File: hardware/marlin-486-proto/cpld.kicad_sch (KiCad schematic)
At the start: 1 part, among them U2 EPM240T100

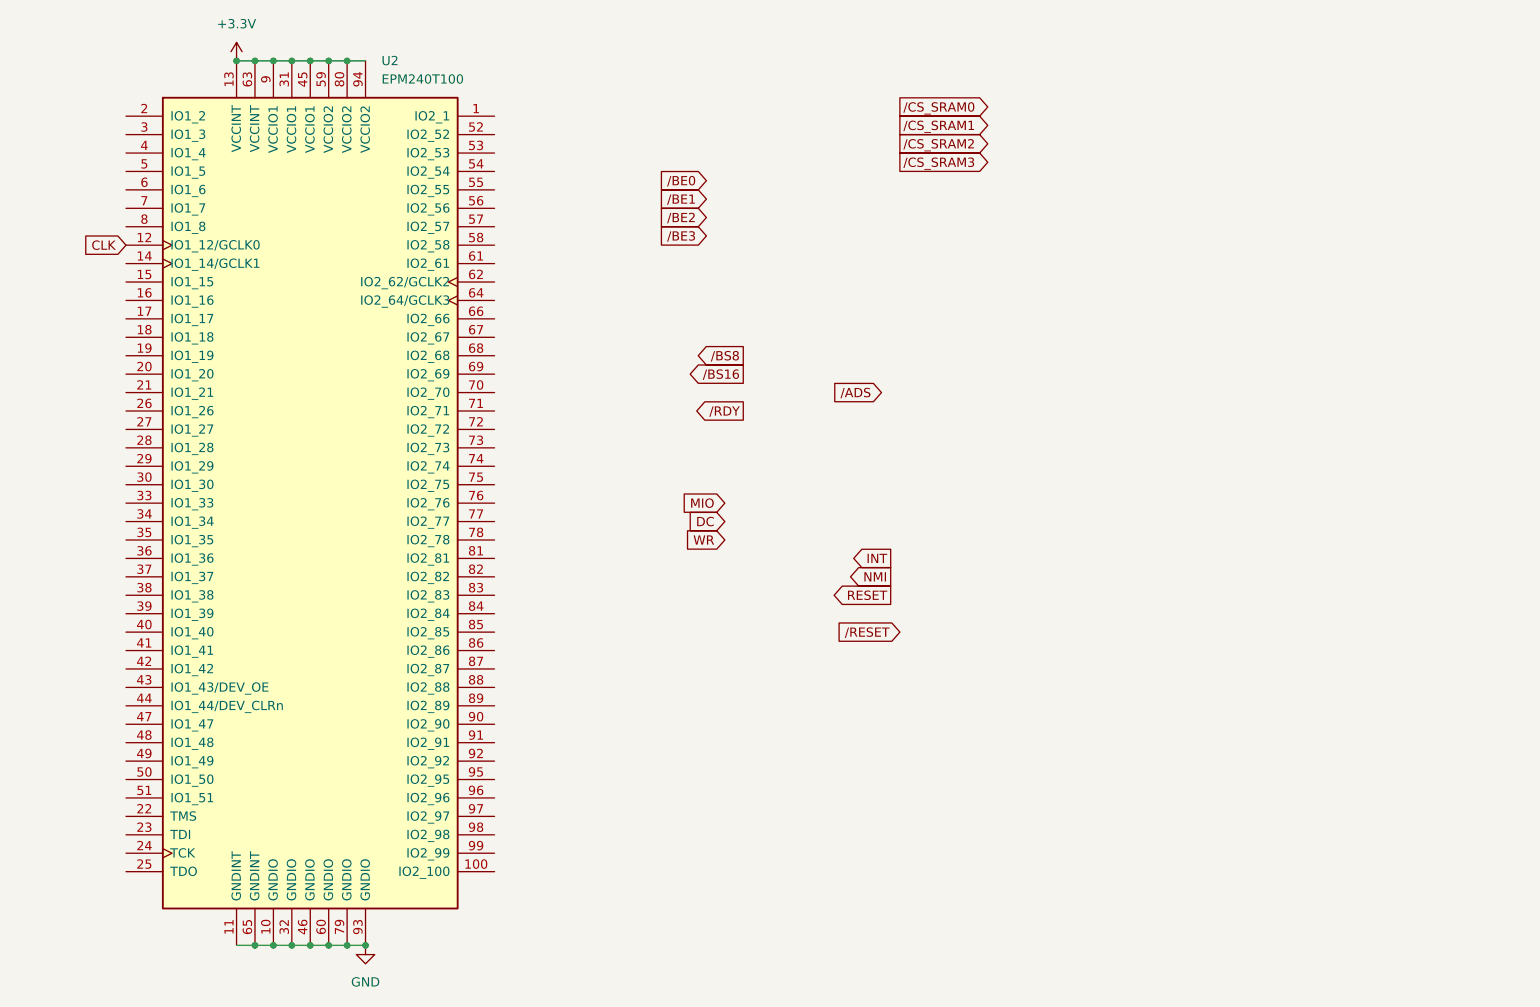
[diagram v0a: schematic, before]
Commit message: Add 16C550 symbol
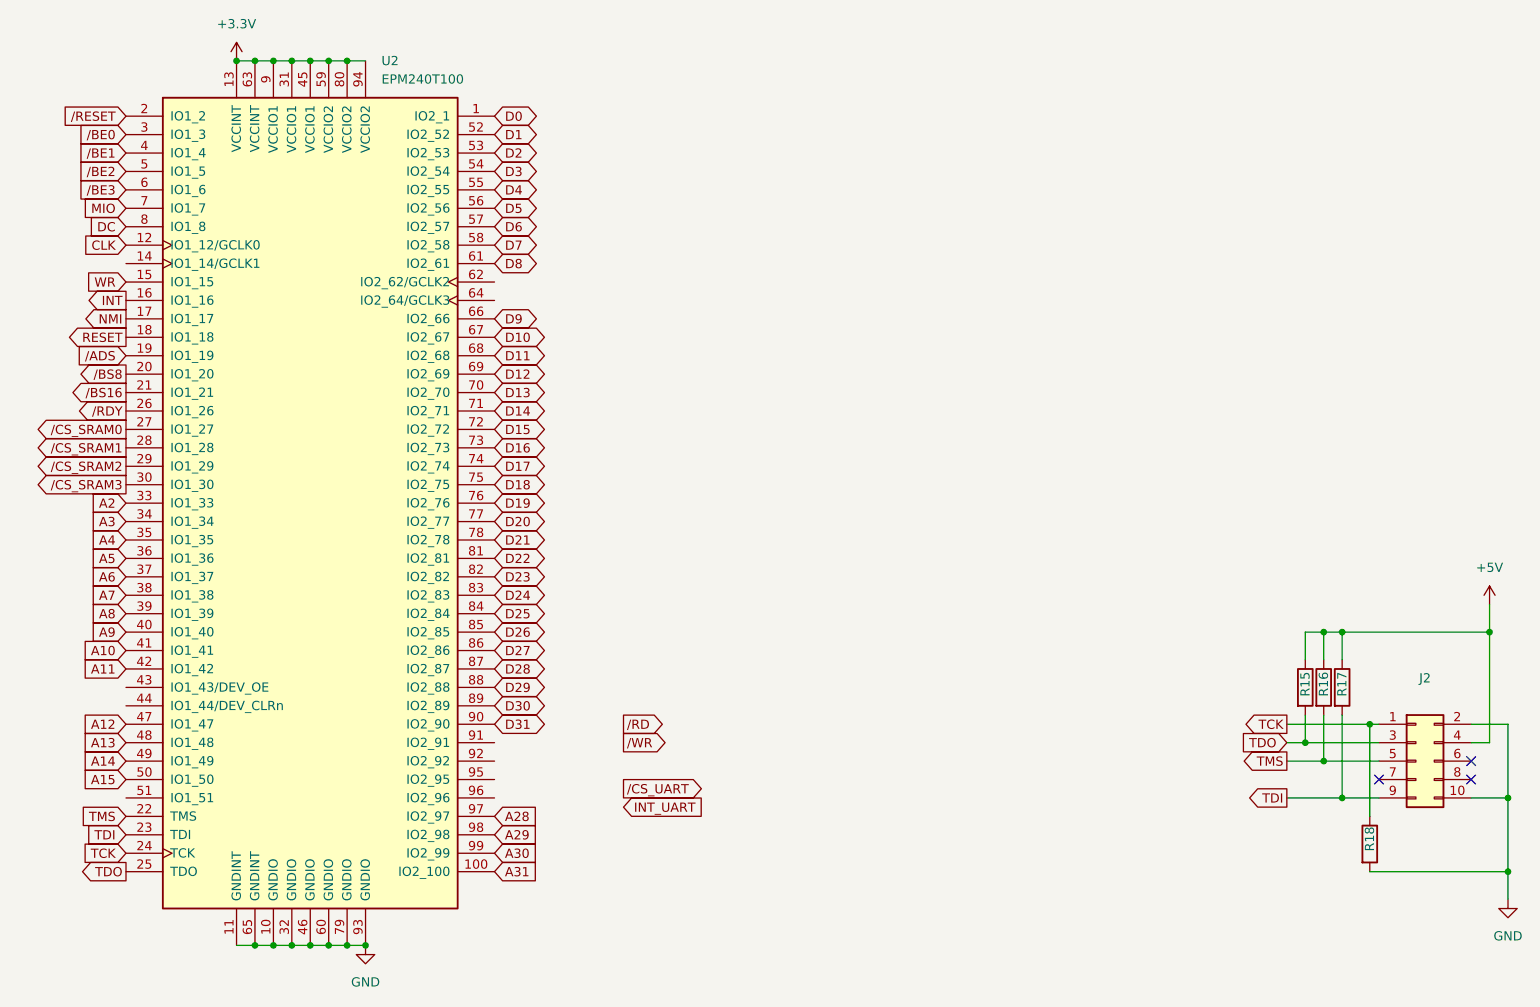
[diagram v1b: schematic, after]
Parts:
- added J2: Conn_02x05_Odd_Even, Connector_IDC:IDC-Header_2x05_P2.54mm_Vertical, symbol Connector_Generic:Conn_02x05_Odd_Even
- added R15, R16, R17, R18: 4k7, Resistor_THT:R_Axial_DIN0207_L6.3mm_D2.5mm_P7.62mm_Horizontal, symbol Device:R
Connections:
- net DC: now also U2.8 (IO1_8)
- net GND: now also J2.10 (Pin_10), J2.2 (Pin_2), R18.2
- net INT: now also U2.16 (IO1_16)
- net MIO: now also U2.7 (IO1_7)
- net NMI: now also U2.17 (IO1_17)
- net RESET: now also U2.18 (IO1_18)
- net WR: now also U2.15 (IO1_15)
- net /ADS: now also U2.19 (IO1_19)
- net /BE0: now also U2.3 (IO1_3)
- net /BE1: now also U2.4 (IO1_4)
- net /BE2: now also U2.5 (IO1_5)
- net /BE3: now also U2.6 (IO1_6)
- net /BS16: now also U2.21 (IO1_21)
- net /BS8: now also U2.20 (IO1_20)
- net /CS_SRAM0: now also U2.27 (IO1_27)
- net /CS_SRAM1: now also U2.28 (IO1_28)
- net /CS_SRAM2: now also U2.29 (IO1_29)
- net /CS_SRAM3: now also U2.30 (IO1_30)
- net /RDY: now also U2.26 (IO1_26)
- net /RESET: now also U2.2 (IO1_2)
- net D0: now reaches U2.1 (IO2_1)
- net A31: now reaches U2.100 (IO2_100)
- net TMS: now reaches U2.22 (TMS)
- net TMS: now also J2.5 (Pin_5), R16.2
- net TDI: now reaches U2.23 (TDI)
- net TDI: now also J2.9 (Pin_9), R17.2
- net TCK: now reaches U2.24 (TCK)
- net TCK: now also J2.1 (Pin_1), R18.1
- net TDO: now reaches U2.25 (TDO)
- net TDO: now also J2.3 (Pin_3), R15.2
- net A2: now reaches U2.33 (IO1_33)
- net A3: now reaches U2.34 (IO1_34)
- net A4: now reaches U2.35 (IO1_35)
- net A5: now reaches U2.36 (IO1_36)
- net A6: now reaches U2.37 (IO1_37)
- net A7: now reaches U2.38 (IO1_38)
- net A8: now reaches U2.39 (IO1_39)
- net A9: now reaches U2.40 (IO1_40)
- net A10: now reaches U2.41 (IO1_41)
- net A11: now reaches U2.42 (IO1_42)
- net A12: now reaches U2.47 (IO1_47)
- net A13: now reaches U2.48 (IO1_48)
- net A14: now reaches U2.49 (IO1_49)
- net A15: now reaches U2.50 (IO1_50)
- net D1: now reaches U2.52 (IO2_52)
- net D2: now reaches U2.53 (IO2_53)
- net D3: now reaches U2.54 (IO2_54)
- net D4: now reaches U2.55 (IO2_55)
- net D5: now reaches U2.56 (IO2_56)
- net D6: now reaches U2.57 (IO2_57)
- net D7: now reaches U2.58 (IO2_58)
- net D8: now reaches U2.61 (IO2_61)
- net D9: now reaches U2.66 (IO2_66)
- net D10: now reaches U2.67 (IO2_67)
- net D11: now reaches U2.68 (IO2_68)
- net D12: now reaches U2.69 (IO2_69)
- net D13: now reaches U2.70 (IO2_70)
- net D14: now reaches U2.71 (IO2_71)
- net D15: now reaches U2.72 (IO2_72)
- net D16: now reaches U2.73 (IO2_73)
- net D17: now reaches U2.74 (IO2_74)
- net D18: now reaches U2.75 (IO2_75)
- net D19: now reaches U2.76 (IO2_76)
- net D20: now reaches U2.77 (IO2_77)
- net D21: now reaches U2.78 (IO2_78)
- net D22: now reaches U2.81 (IO2_81)
- net D23: now reaches U2.82 (IO2_82)
- net D24: now reaches U2.83 (IO2_83)
- net D25: now reaches U2.84 (IO2_84)
- net D26: now reaches U2.85 (IO2_85)
- net D27: now reaches U2.86 (IO2_86)
- net D28: now reaches U2.87 (IO2_87)
- net D29: now reaches U2.88 (IO2_88)
- net D30: now reaches U2.89 (IO2_89)
- net D31: now reaches U2.90 (IO2_90)
- net A28: now reaches U2.97 (IO2_97)
- net A29: now reaches U2.98 (IO2_98)
- net A30: now reaches U2.99 (IO2_99)
- new net +5V: J2.4 (Pin_4), R15.1, R16.1, R17.1
- no-connect marks 0 -> 3
